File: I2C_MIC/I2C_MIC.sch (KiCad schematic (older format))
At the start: 6 parts, among them J1 I2S_PMOD, U1 SPH0645LM4H-B

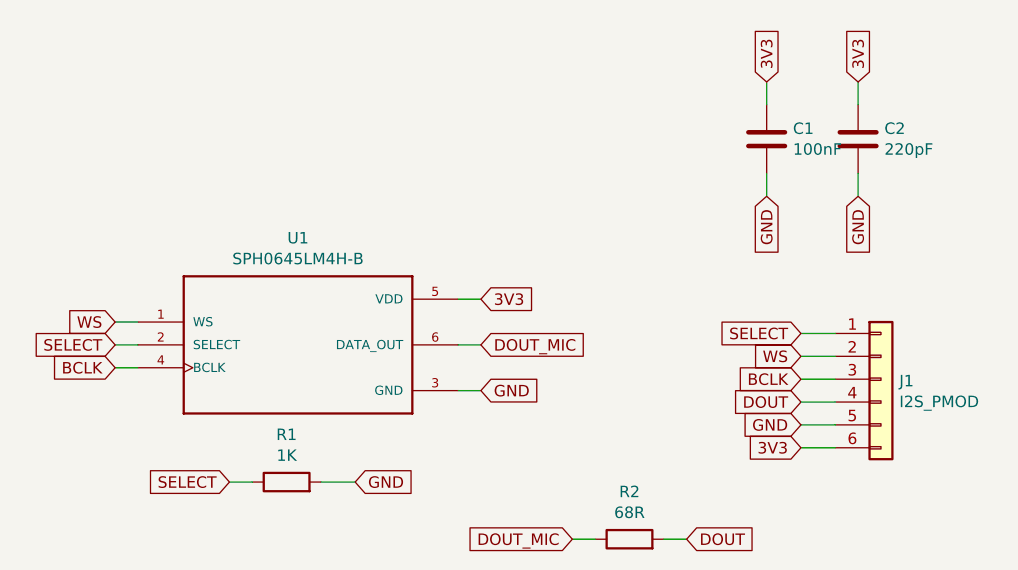
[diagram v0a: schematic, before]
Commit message: Fixing I2S-MIC
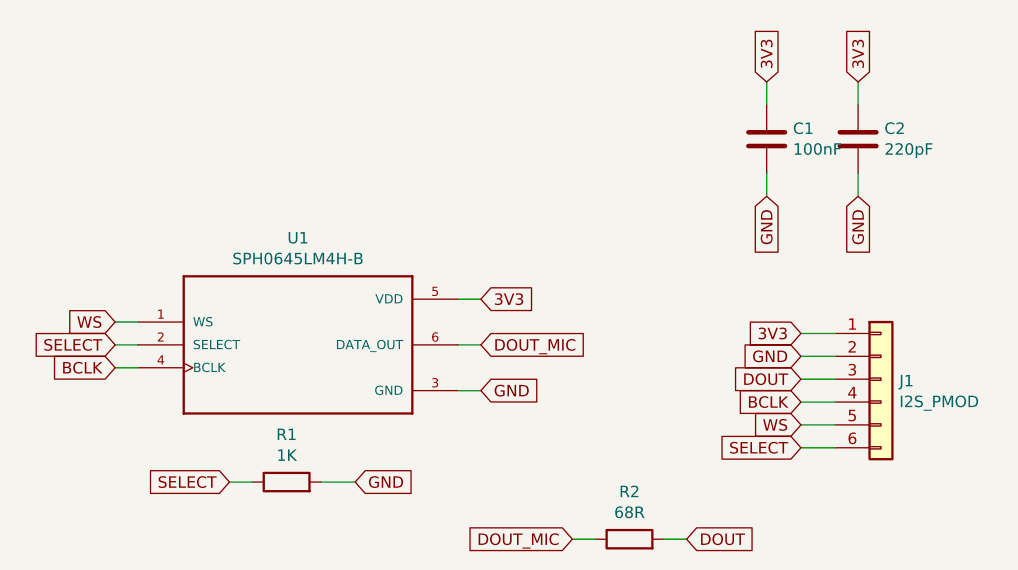
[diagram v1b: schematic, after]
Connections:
- net 3V3: now also J1.1 (Pin_1); no longer J1.6 (Pin_6)
- net BCLK: now also J1.4 (Pin_4); no longer J1.3 (Pin_3)
- net DOUT: now also J1.3 (Pin_3); no longer J1.4 (Pin_4)
- net GND: now also J1.2 (Pin_2); no longer J1.5 (Pin_5)
- net SELECT: now also J1.6 (Pin_6); no longer J1.1 (Pin_1)
- net WS: now also J1.5 (Pin_5); no longer J1.2 (Pin_2)
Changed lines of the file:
@@
 EESchema Schematic File Version 4
+LIBS:I2C_MIC-cache
 EELAYER 26 0
 EELAYER END
@@
 	1    0    0    -1
 $EndComp
+Text GLabel 8000 3500 0    50   Input ~ 0
+3V3
+Text GLabel 8000 3600 0    50   Input ~ 0
+GND
+Text GLabel 8000 3800 0    50   Input ~ 0
+BCLK
+Text GLabel 8000 3700 0    50   Input ~ 0
+DOUT
+Text GLabel 8000 3900 0    50   Input ~ 0
+WS
 Text GLabel 8000 4000 0    50   Input ~ 0
-3V3
-Text GLabel 8000 3900 0    50   Input ~ 0
-GND
-Text GLabel 8000 3700 0    50   Input ~ 0
-BCLK
-Text GLabel 8000 3800 0    50   Input ~ 0
-DOUT
-Text GLabel 8000 3600 0    50   Input ~ 0
-WS
-Text GLabel 8000 3500 0    50   Input ~ 0
 SELECT
 Wire Wire Line
